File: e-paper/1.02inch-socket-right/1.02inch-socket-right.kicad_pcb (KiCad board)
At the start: 2 copper layers, 10.4 x 1 mm, 7 parts

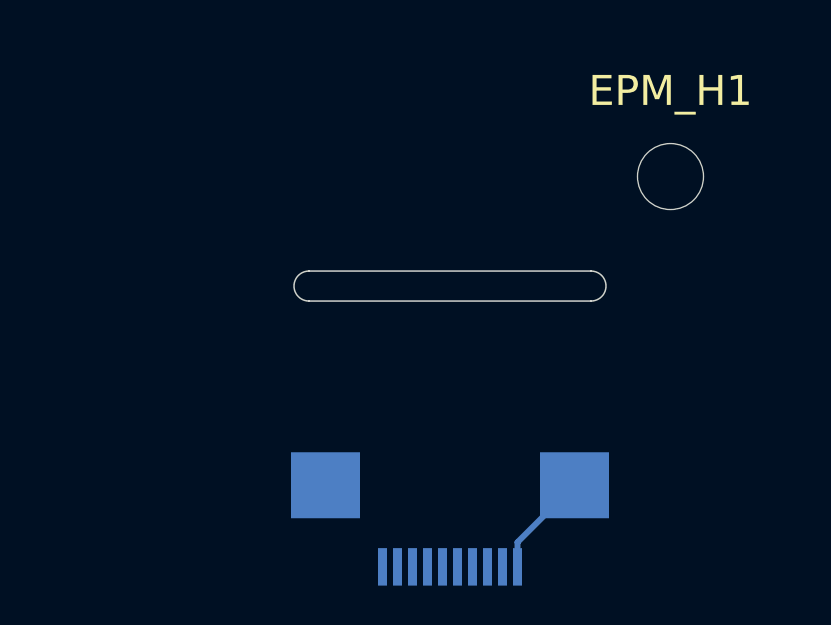
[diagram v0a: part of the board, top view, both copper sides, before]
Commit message: remove gap between e-paper hole and mount
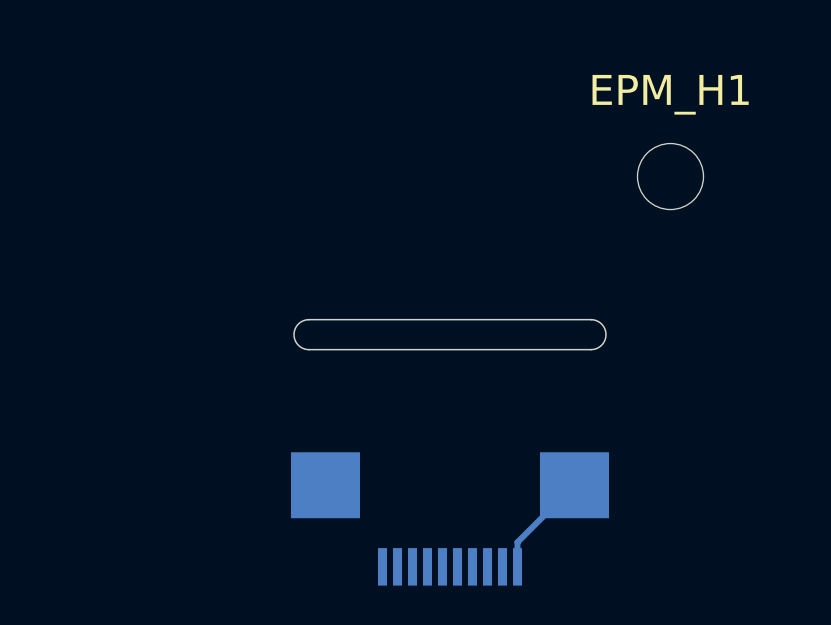
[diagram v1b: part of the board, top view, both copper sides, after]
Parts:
- moved EPM_GAP1 1.62 mm to (10.5, -6.38)
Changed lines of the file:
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@@
 	(footprint "ErgoCai.pretty:e-paper_1.02inch_gap"
 		(layer "F.Cu")
-		(at 10.5 -8)
+		(at 10.5 -6.38)
 		(property "Reference" "EPM_GAP1"
 			(at 0 -0.5 0)

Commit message: update TP4056 charger
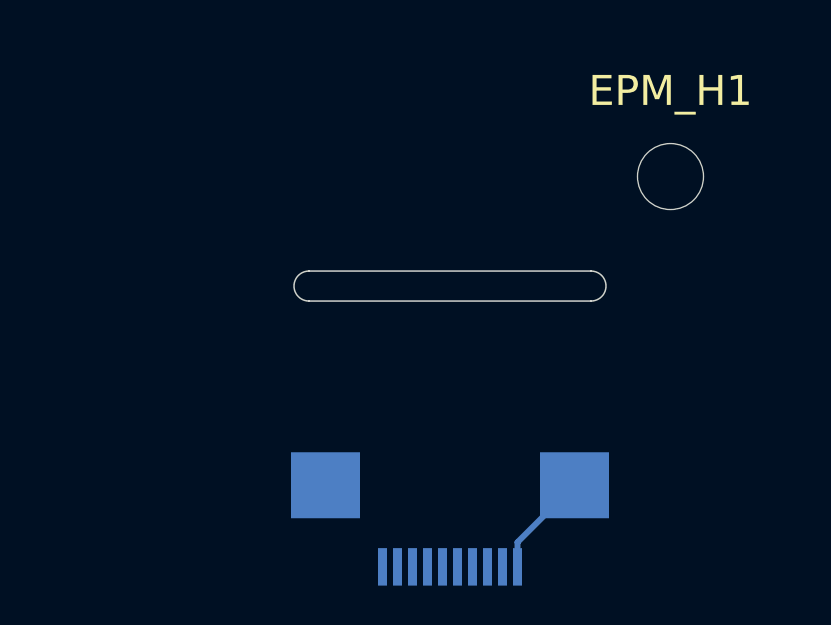
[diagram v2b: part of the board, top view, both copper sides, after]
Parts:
- moved EPM_GAP1 1.62 mm to (10.5, -8.00)
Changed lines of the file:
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@@
 	(footprint "ErgoCai.pretty:e-paper_1.02inch_gap"
 		(layer "F.Cu")
-		(at 10.5 -6.38)
+		(at 10.5 -8)
 		(property "Reference" "EPM_GAP1"
 			(at 0 -0.5 0)
